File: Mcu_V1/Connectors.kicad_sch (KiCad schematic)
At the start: 4 parts, among them J1 Conn_01x04_Pin, J2 Conn_01x04_Pin, J3 Conn_01x09_Pin, J4 Conn_02x03_Odd_Even

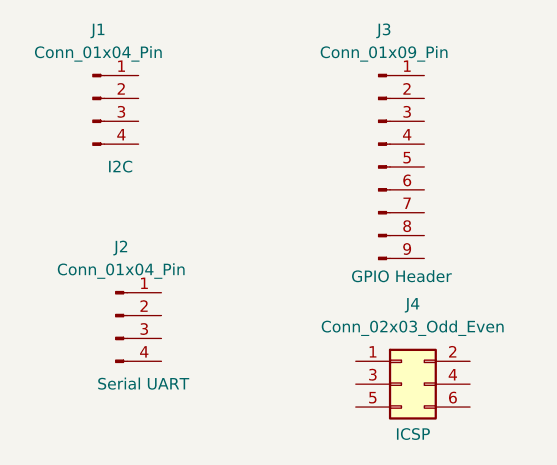
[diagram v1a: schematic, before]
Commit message: wiring done
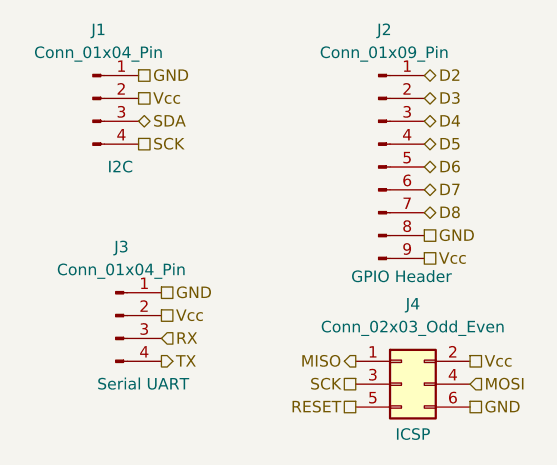
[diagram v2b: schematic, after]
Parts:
- J1: footprint (none) -> Connector_PinHeader_2.54mm:PinHeader_1x04_P2.54mm_Vertical
- J2: renamed from J3; footprint (none) -> Connector_PinHeader_2.54mm:PinHeader_1x09_P2.54mm_Vertical
- J3: renamed from J2; footprint (none) -> Connector_PinHeader_2.54mm:PinHeader_1x04_P2.54mm_Vertical
- J4: footprint (none) -> Connector_PinHeader_2.54mm:PinHeader_2x03_P2.54mm_Vertical
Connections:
- net D2: now reaches J2.1 (Pin_1)
- net D3: now reaches J2.2 (Pin_2)
- net D4: now reaches J2.3 (Pin_3)
- net D5: now reaches J2.4 (Pin_4)
- net D6: now reaches J2.5 (Pin_5)
- net D7: now reaches J2.6 (Pin_6)
- net D8: now reaches J2.7 (Pin_7)
- net GND: now reaches J2.8 (Pin_8)
- net GND: now also J1.1 (Pin_1), J3.1 (Pin_1), J4.6 (Pin_6)
- net Vcc: now reaches J2.9 (Pin_9)
- net Vcc: now also J1.2 (Pin_2), J3.2 (Pin_2), J4.2 (Pin_2)
- net RX: now reaches J3.3 (Pin_3)
- net TX: now reaches J3.4 (Pin_4)
- net MISO: now reaches J4.1 (Pin_1)
- net SCK: now reaches J4.3 (Pin_3)
- net SCK: now also J1.4 (Pin_4)
- net MOSI: now reaches J4.4 (Pin_4)
- net RESET: now reaches J4.5 (Pin_5)
- net SDA: now reaches J1.3 (Pin_3)
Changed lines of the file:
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@@
 	(generator_version "9.0")
 	(paper "A4")
+	(hierarchical_label "Vcc"
+		(shape passive)
+		(at 86.36 44.45 0)
+		(effects
+			(font
+				(size 1.27 1.27)
+			)
+			(justify left)
+		)
+	)
+	(hierarchical_label "TX"
+		(shape output)
+		(at 88.9 73.66 0)
+		(effects
+			(font
+				(size 1.27 1.27)
+			)
+			(justify left)
+		)
+	)
+	(hierarchical_label "Vcc"
+		(shape passive)
+		(at 88.9 68.58 0)
+		(effects
+			(font
+				(size 1.27 1.27)
+			)
+			(justify left)
+		)
+	)
+	(hierarchical_label "GND"
+		(shape passive)
+		(at 123.19 78.74 0)
+		(effects
+			(font
+				(size 1.27 1.27)
+			)
+			(justify left)
+		)
+	)
+	(hierarchical_label "MOSI"
+		(shape input)
+		(at 123.19 76.2 0)
+		(effects
+			(font
+				(size 1.27 1.27)
+			)
+			(justify left)
+		)
+	)
+	(hierarchical_label "D2"
+		(shape bidirectional)
+		(at 118.11 41.91 0)
+		(effects
+			(font
+				(size 1.27 1.27)
+			)
+			(justify left)
+		)
+	)
+	(hierarchical_label "GND"
+		(shape passive)
+		(at 118.11 59.69 0)
+		(effects
+			(font
+				(size 1.27 1.27)
+			)
+			(justify left)
+		)
+	)
+	(hierarchical_label "RX"
+		(shape input)
+		(at 88.9 71.12 0)
+		(effects
+			(font
+				(size 1.27 1.27)
+			)
+			(justify left)
+		)
+	)
+	(hierarchical_label "MISO"
+		(shape output)
+		(at 110.49 73.66 180)
+		(effects
+			(font
+				(size 1.27 1.27)
+			)
+			(justify right)
+		)
+	)
+	(hierarchical_label "D8"
+		(shape bidirectional)
+		(at 118.11 57.15 0)
+		(effects
+			(font
+				(size 1.27 1.27)
+			)
+			(justify left)
+		)
+	)
+	(hierarchical_label "RESET"
+		(shape passive)
+		(at 110.49 78.74 180)
+		(effects
+			(font
+				(size 1.27 1.27)
+			)
+			(justify right)
+		)
+	)
+	(hierarchical_label "SCK"
+		(shape passive)
+		(at 86.36 49.53 0)
+		(effects
+			(font
+				(size 1.27 1.27)
+			)
+			(justify left)
+		)
+	)
+	(hierarchical_label "D7"
+		(shape bidirectional)
+		(at 118.11 54.61 0)
+		(effects
+			(font
+				(size 1.27 1.27)
+			)
+			(justify left)
+		)
+	)
+	(hierarchical_label "GND"
+		(shape passive)
+		(at 86.36 41.91 0)
+		(effects
+			(font
+				(size 1.27 1.27)
+			)
+			(justify left)
+		)
+	)
+	(hierarchical_label "Vcc"
+		(shape passive)
+		(at 123.19 73.66 0)
+		(effects
+			(font
+				(size 1.27 1.27)
+			)
+			(justify left)
+		)
+	)
+	(hierarchical_label "SDA"
+		(shape bidirectional)
+		(at 86.36 46.99 0)
+		(effects
+			(font
+				(size 1.27 1.27)
+			)
+			(justify left)
+		)
+	)
+	(hierarchical_label "GND"
+		(shape passive)
+		(at 88.9 66.04 0)
+		(effects
+			(font
+				(size 1.27 1.27)
+			)
+			(justify left)
+		)
+	)
+	(hierarchical_label "SCK"
+		(shape passive)
+		(at 110.49 76.2 180)
+		(effects
+			(font
+				(size 1.27 1.27)
+			)
+			(justify right)
+		)
+	)
+	(hierarchical_label "D5"
+		(shape bidirectional)
+		(at 118.11 49.53 0)
+		(effects
+			(font
+				(size 1.27 1.27)
+			)
+			(justify left)
+		)
+	)
+	(hierarchical_label "D3"
+		(shape bidirectional)
+		(at 118.11 44.45 0)
+		(effects
+			(font
+				(size 1.27 1.27)
+			)
+			(justify left)
+		)
+	)
+	(hierarchical_label "D6"
+		(shape bidirectional)
+		(at 118.11 52.07 0)
+		(effects
+			(font
+				(size 1.27 1.27)
+			)
+			(justify left)
+		)
+	)
+	(hierarchical_label "D4"
+		(shape bidirectional)
+		(at 118.11 46.99 0)
+		(effects
+			(font
+				(size 1.27 1.27)
+			)
+			(justify left)
+		)
+	)
+	(hierarchical_label "Vcc"
+		(shape passive)
+		(at 118.11 62.23 0)
+		(effects
+			(font
+				(size 1.27 1.27)
+			)
+			(justify left)
+		)
+	)
 	(symbol
 		(lib_id "Connector:Conn_01x09_Pin")
@@
 		(on_board yes)
 		(dnp no)
-		(property "Reference" "J3"
+		(property "Reference" "J2"
 			(at 113.665 36.83 0)
 			(effects
@@
 			)
 		)
-		(property "Footprint" ""
+		(property "Footprint" "Connector_PinHeader_2.54mm:PinHeader_1x09_P2.54mm_Vertical"
 			(at 113.03 52.07 0)
 			(effects
@@
 			(project ""
 				(path "/8a20ec19-5ddc-4fb8-87e4-eca44506b4b3/1098b824-b392-40d5-8ded-eb67ffdfb450"
-					(reference "J3")
+					(reference "J2")
 					(unit 1)
 				)
@@
 		(on_board yes)
 		(dnp no)
-		(property "Reference" "J2"
+		(property "Reference" "J3"
 			(at 84.455 60.96 0)
 			(effects
@@
 			)
 		)
-		(property "Footprint" ""
+		(property "Footprint" "Connector_PinHeader_2.54mm:PinHeader_1x04_P2.54mm_Vertical"
 			(at 83.82 68.58 0)
 			(effects
@@
 			(project "Mcu_V1"
 				(path "/8a20ec19-5ddc-4fb8-87e4-eca44506b4b3/1098b824-b392-40d5-8ded-eb67ffdfb450"
-					(reference "J2")
+					(reference "J3")
 					(unit 1)
 				)
@@
 			)
 		)
-		(property "Footprint" ""
+		(property "Footprint" "Connector_PinHeader_2.54mm:PinHeader_2x03_P2.54mm_Vertical"
 			(at 115.57 76.2 0)
 			(effects
@@
 			)
 		)
-		(property "Footprint" ""
+		(property "Footprint" "Connector_PinHeader_2.54mm:PinHeader_1x04_P2.54mm_Vertical"
 			(at 81.28 44.45 0)
 			(effects
